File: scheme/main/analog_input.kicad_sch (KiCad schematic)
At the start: 0 parts

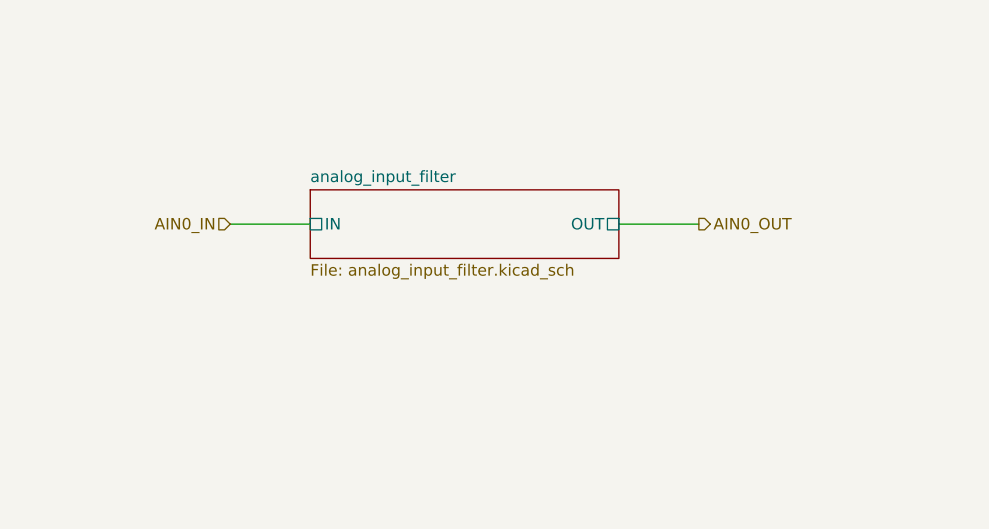
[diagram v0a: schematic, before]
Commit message: analog input 0 schematic modified
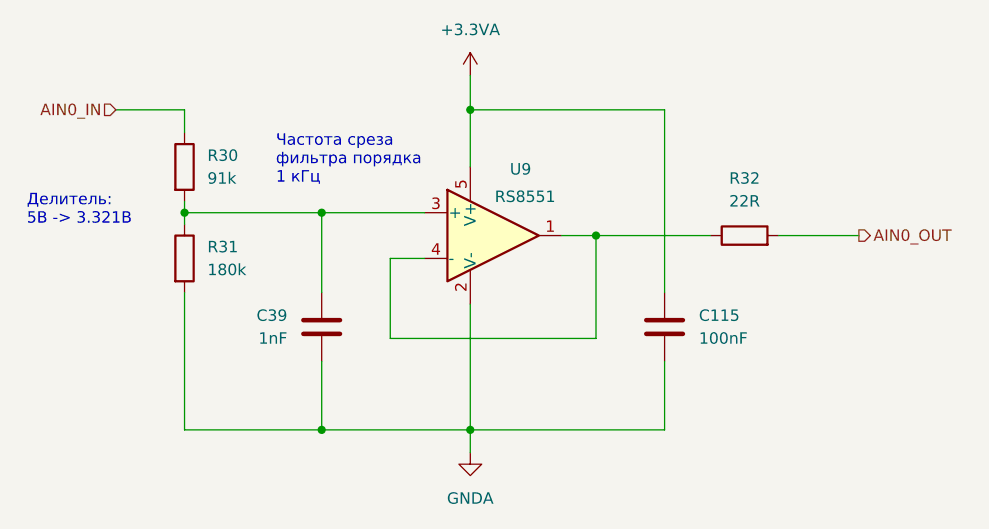
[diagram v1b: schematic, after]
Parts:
- added C115: 100nF, Capacitor_SMD:C_0805_2012Metric, symbol Device:C
- added C39: 1nF, Capacitor_SMD:C_0805_2012Metric, symbol Device:C
- added R30: 91k, Resistor_SMD:R_0805_2012Metric, symbol Device:R
- added R31: 180k, Resistor_SMD:R_0805_2012Metric, symbol Device:R
- added R32: 22R, Resistor_SMD:R_0805_2012Metric, symbol Device:R
- added U9: RS8551, Package_TO_SOT_SMD:TSOT-23-5, symbol main:RS8551
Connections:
- net AIN0_IN: now also R30.1
- net AIN0_OUT: now also R32.2
- new net: C39.2, R30.2, R31.1, U9.3 (+)
- new net: R32.1, U9.1, U9.4 (-)
- new net +3.3VA: C115.1, U9.5 (V+)
- new net GNDA: C115.2, C39.1, R31.2, U9.2 (V-)
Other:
- removed sheet analog_input_filter
- note added: "Делитель: 5В -> 3.321В"
- note added: "Частота среза фильтра порядка 1 кГц"
